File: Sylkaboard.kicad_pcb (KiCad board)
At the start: 2 copper layers, 149.6 x 125.6 mm, 117 parts, among them J1 Conn_01x04_Pin, J2 USB_C_Receptacle_USB2.0_16P, U1 RP2040-ZERO

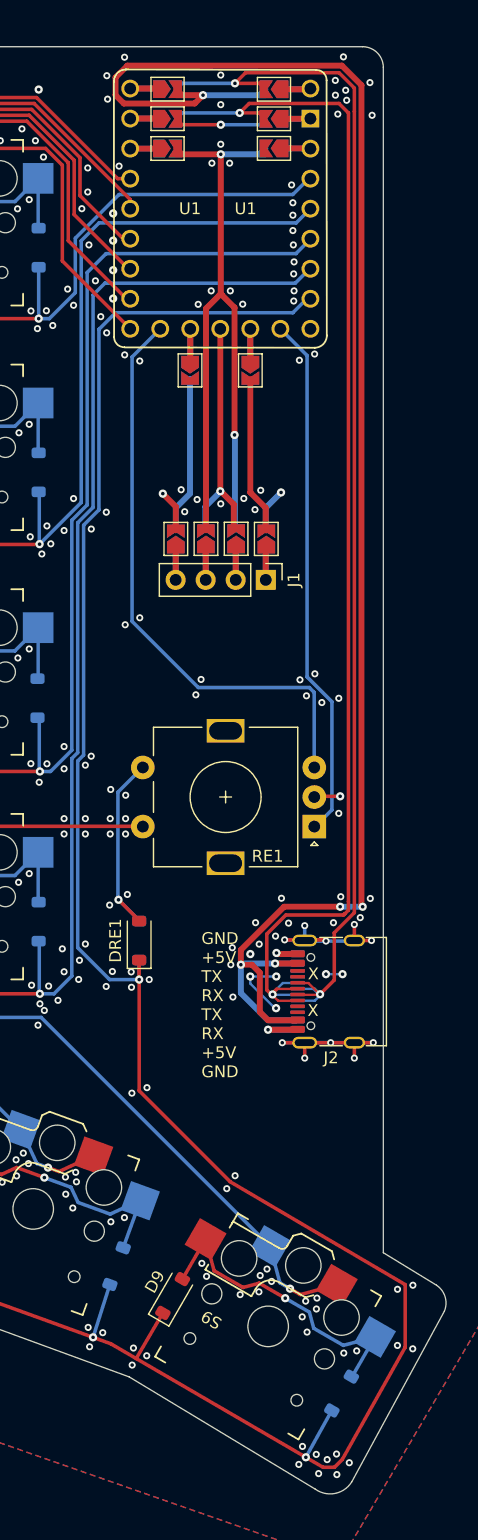
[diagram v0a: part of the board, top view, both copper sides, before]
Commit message: swap usb-c connector and rotary encoder
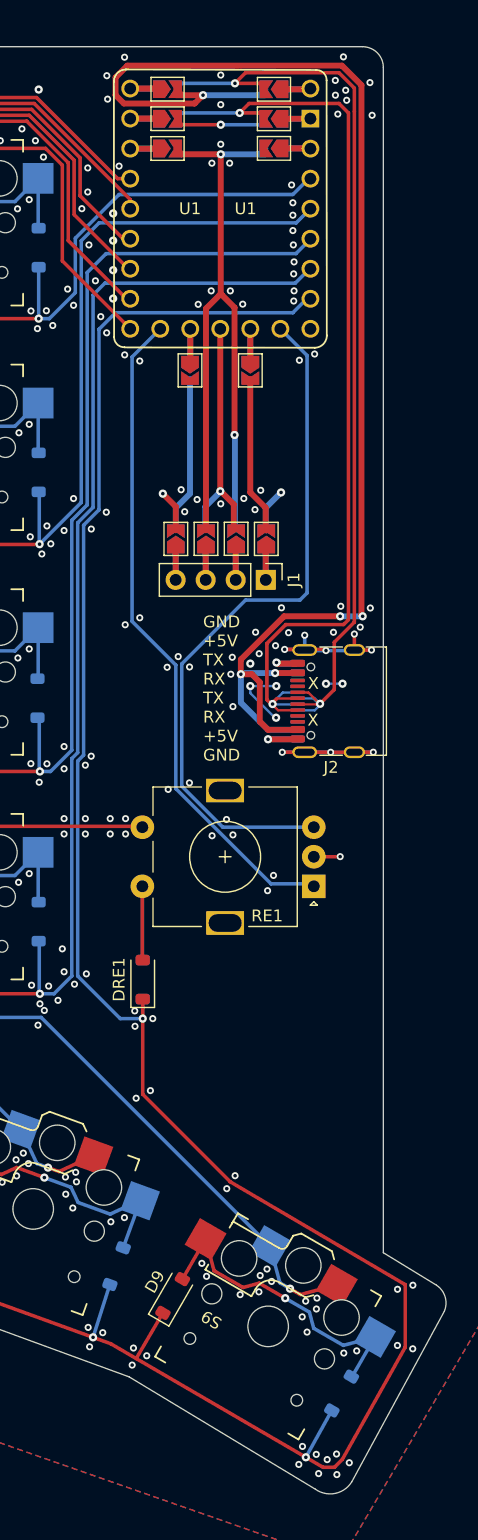
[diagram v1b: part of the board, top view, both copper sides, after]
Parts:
- moved J2 24.6 mm to (249.7, 156.8)
- moved RE1 5.05 mm to (247.4, 172.5)
- moved DRE1 3.31 mm to (232.9, 180.4)
- moved DRE101 3.31 mm to (232.9, 180.4)
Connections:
- RE1 pad A: /encA -> /encB
- RE1 pad B: /encB -> /encA
- RE1 pad S1: /RED1 -> /col6
- RE1 pad S2: /col6 -> /RED1
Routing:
- net /RX: track 108.7 -> 84.2 mm
- net +5V: track 146.3 -> 121.7 mm
- net /TX: track 106.3 -> 81.7 mm
- net /encA: track 44.5 -> 59.3 mm
- net /encB: track 49.8 -> 56.2 mm
- net /RED1: track 17.2 -> 12.4 mm, vias 1 -> 0
- net GND: track 65.6 -> 63.2 mm, vias 973 -> 966

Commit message: rotary encoder adjustements
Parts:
- moved D114 1.39 mm to (231.7, 205.6)
- moved D14 1.39 mm to (216.1, 200.2)
- moved S14 1.39 mm to (224.7, 200.7)
- moved DRE1 0.45 mm to (232.6, 180.1)
- moved DRE101 0.45 mm to (232.6, 180.1)
- moved RE1 0.45 mm to (247.1, 172.2)
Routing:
- net GND: track 63.2 -> 62.8 mm, vias 966 -> 963

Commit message: inverted encoder pins (A and B) on schematic
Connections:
- RE1 pad A: /encB -> /encA
- RE1 pad B: /encA -> /encB
- U1 pad 10: /encB -> /encA
- U1 pad 14: /encA -> /encB
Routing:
- net /encB: track 56.5 -> 59.6 mm
- net /encA: track 59.6 -> 56.5 mm
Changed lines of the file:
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@@
 			(layers "*.Cu" "*.Mask")
 			(remove_unused_layers no)
-			(net "/encB")
+			(net "/encA")
 			(pinfunction "A_A")
 			(pintype "passive")
@@
 			(layers "*.Cu" "*.Mask")
 			(remove_unused_layers no)
-			(net "/encA")
+			(net "/encB")
 			(pinfunction "B_B")
 			(pintype "passive")
@@
 			(layers "*.Cu" "*.Mask")
 			(remove_unused_layers no)
-			(net "/encB")
+			(net "/encA")
 			(pinfunction "GP9_10")
 			(pintype "bidirectional")
@@
 			(layers "*.Cu" "*.Mask")
 			(remove_unused_layers no)
-			(net "/encA")
+			(net "/encB")
 			(pinfunction "GP13_14")
 			(pintype "bidirectional")
@@
 	)
 	(segment
-		(start 246.838672 171.988672)
-		(end 242.158672 171.988672)
+		(start 244.5425 125.36)
+		(end 246.8 127.6175)
 		(width 0.3)
 		(layer "B.Cu")
@@
 	)
 	(segment
-		(start 232 127.7425)
-		(end 234.3825 125.36)
+		(start 238.077106 167.2)
+		(end 247.05 167.2)
 		(width 0.3)
 		(layer "B.Cu")
@@
 	)
 	(segment
-		(start 235.7 165.53)
-		(end 235.7 153.8)
+		(start 236.2 153.7)
+		(end 236.2 165.322894)
 		(width 0.3)
 		(layer "B.Cu")
@@
 	)
 	(segment
-		(start 242.158672 171.988672)
-		(end 235.7 165.53)
+		(start 246.8 147.7)
+		(end 246.2 148.3)
 		(width 0.3)
 		(layer "B.Cu")
@@
 	)
 	(segment
-		(start 235.7 153.8)
-		(end 232 150.1)
+		(start 246.8 127.6175)
+		(end 246.8 147.7)
 		(width 0.3)
 		(layer "B.Cu")
@@
 	)
 	(segment
-		(start 232 150.1)
-		(end 232 127.7425)
+		(start 241.6 148.3)
+		(end 236.2 153.7)
 		(width 0.3)
 		(layer "B.Cu")
@@
 	)
 	(segment
-		(start 244.5425 125.36)
-		(end 246.8 127.6175)
+		(start 246.2 148.3)
+		(end 241.6 148.3)
 		(width 0.3)
 		(layer "B.Cu")
-		(net "/encA")
+		(net "/encB")
 	)
 	(segment
-		(start 238.077106 167.2)
-		(end 247.05 167.2)
+		(start 236.2 165.322894)
+		(end 238.077106 167.2)
 		(width 0.3)
 		(layer "B.Cu")
-		(net "/encA")
+		(net "/encB")
 	)
 	(segment
-		(start 236.2 153.7)
-		(end 236.2 165.322894)
+		(start 246.838672 171.988672)
+		(end 242.158672 171.988672)
 		(width 0.3)
 		(layer "B.Cu")
@@
 	)
 	(segment
-		(start 246.8 147.7)
-		(end 246.2 148.3)
+		(start 232 127.7425)
+		(end 234.3825 125.36)
 		(width 0.3)
 		(layer "B.Cu")
@@
 	)
 	(segment
-		(start 246.8 127.6175)
-		(end 246.8 147.7)
+		(start 235.7 165.53)
+		(end 235.7 153.8)
 		(width 0.3)
 		(layer "B.Cu")
@@
 	)
 	(segment
-		(start 241.6 148.3)
-		(end 236.2 153.7)
+		(start 242.158672 171.988672)
+		(end 235.7 165.53)
 		(width 0.3)
 		(layer "B.Cu")
@@
 	)
 	(segment
-		(start 246.2 148.3)
-		(end 241.6 148.3)
+		(start 235.7 153.8)
+		(end 232 150.1)
 		(width 0.3)
 		(layer "B.Cu")
@@
 	)
 	(segment
-		(start 236.2 165.322894)
-		(end 238.077106 167.2)
+		(start 232 150.1)
+		(end 232 127.7425)
 		(width 0.3)
 		(layer "B.Cu")

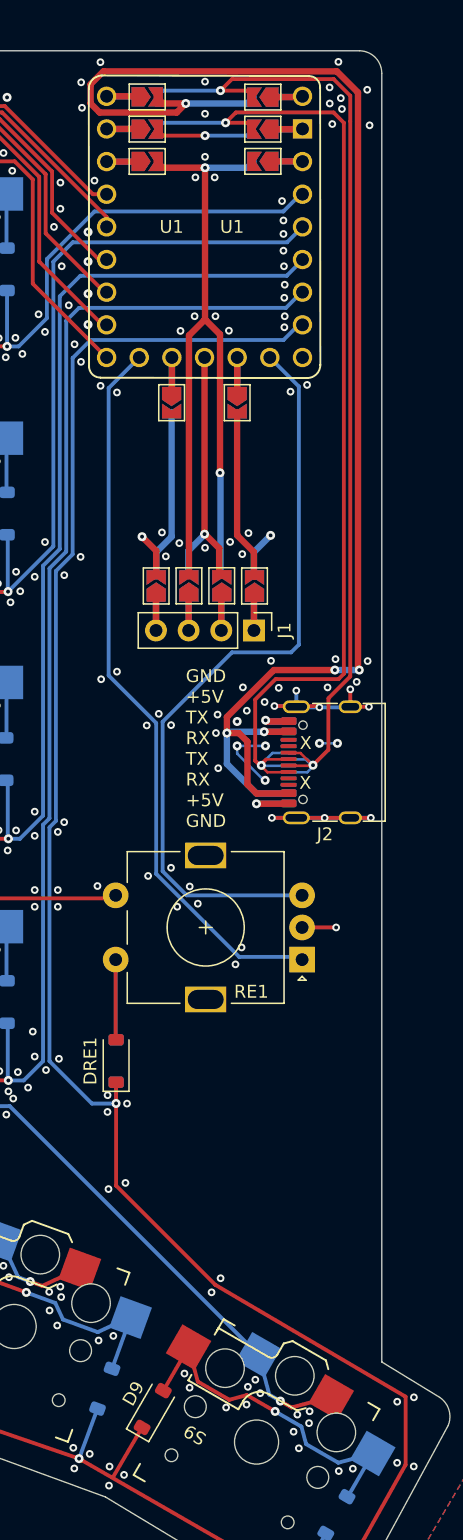
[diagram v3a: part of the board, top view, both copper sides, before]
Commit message: rx tx of the same length
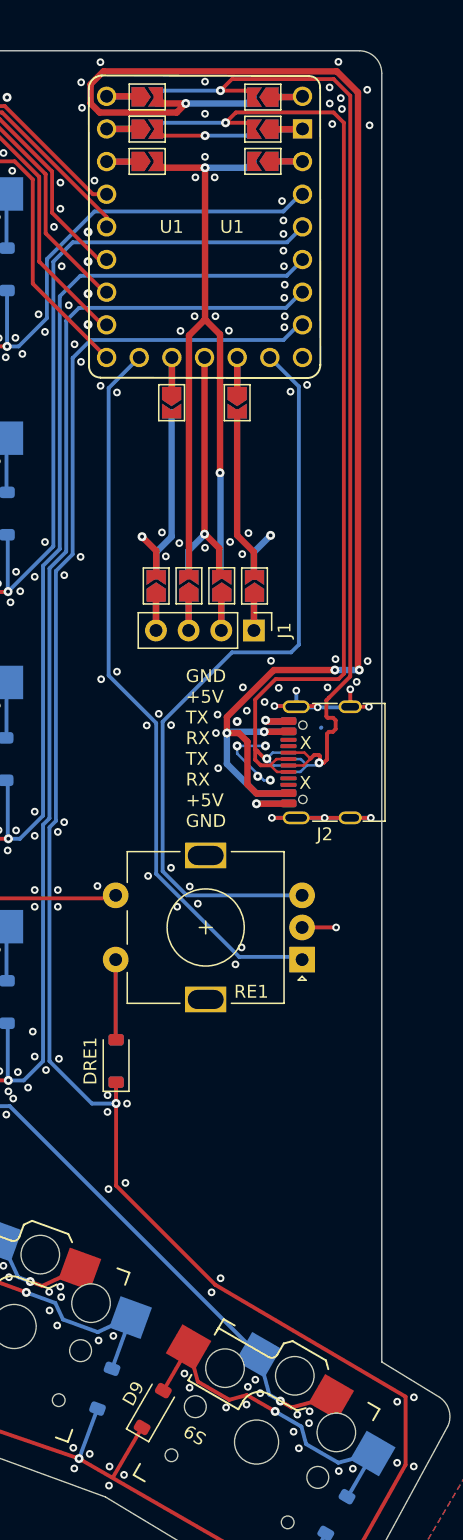
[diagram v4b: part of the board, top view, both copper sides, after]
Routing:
- net /TX: track 81.7 -> 83.7 mm
- net GND: track 62.8 -> 61.8 mm, vias 963 -> 962
